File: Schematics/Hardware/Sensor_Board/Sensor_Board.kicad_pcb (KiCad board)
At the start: 2 copper layers, 115.5 x 152.7 mm, 99 parts, among them J1 Conn_02x13_Odd_Even, J2 Conn_02x20_Odd_Even, U1 CAP1188-1-CP-TR, U2 CAP1188-1-CP-TR, U3 CAP1188-1-CP-TR, U4 LCD

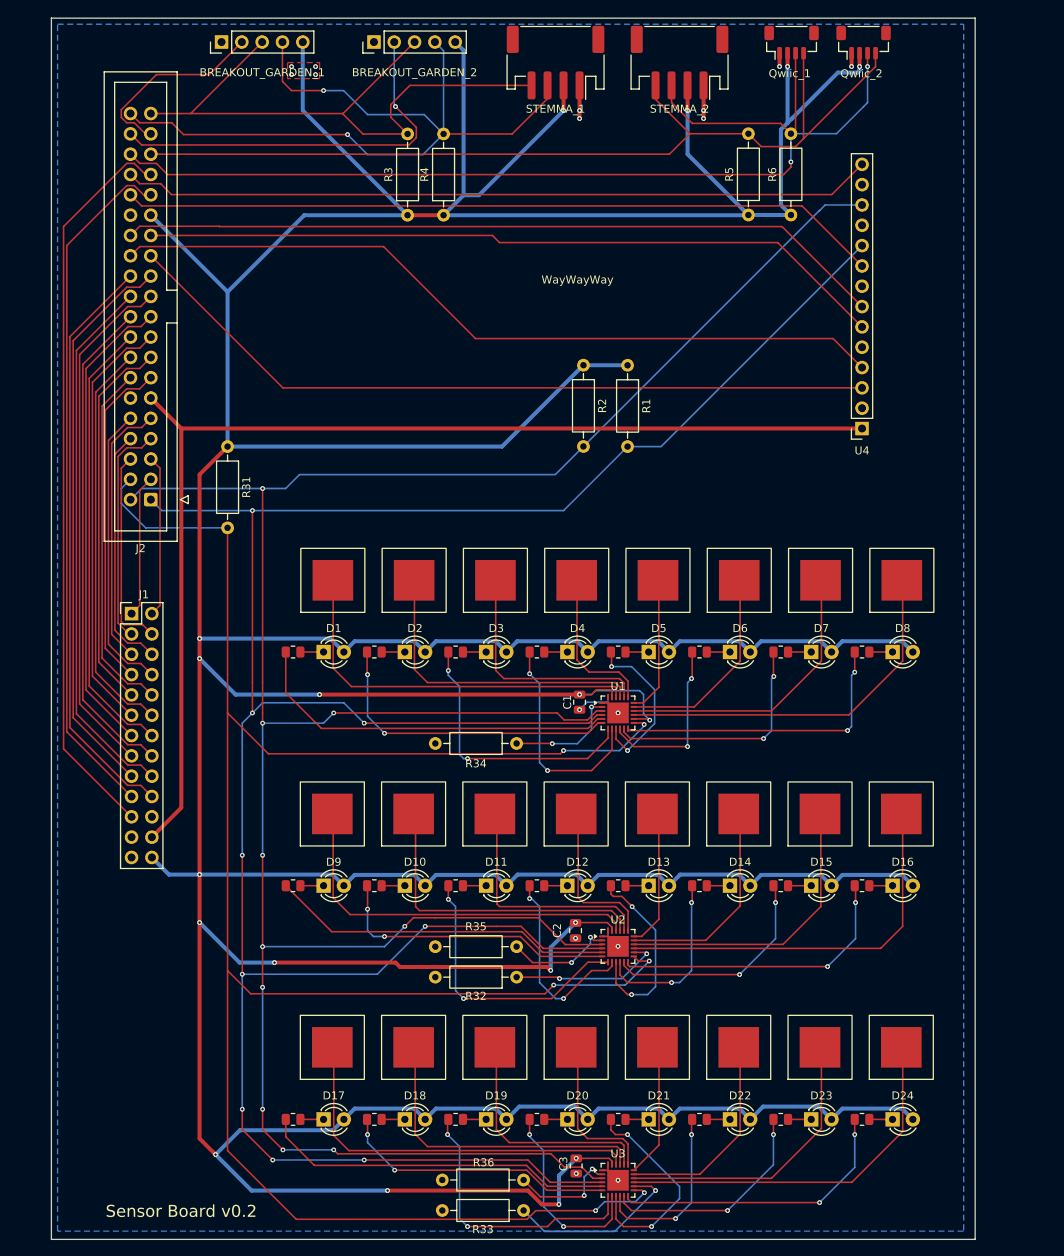
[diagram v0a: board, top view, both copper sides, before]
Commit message: Updated Sensor board schematic/PCB
Still need to double check STEMMA connector and LCD standoff placement.
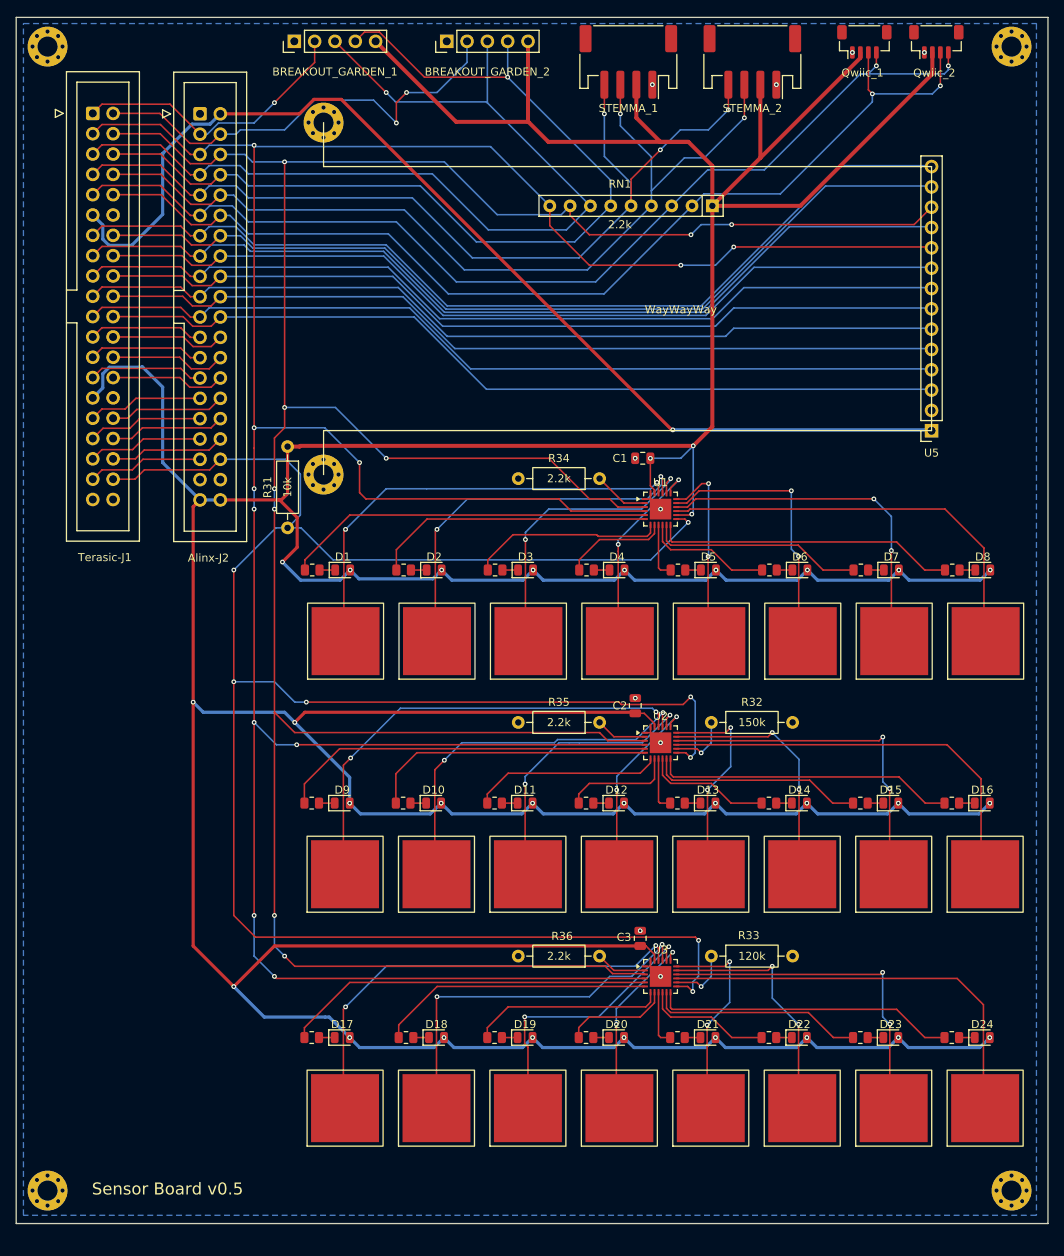
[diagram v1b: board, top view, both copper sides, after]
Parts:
- removed J1: Conn_02x13_Odd_Even, Connector_PinHeader_2.54mm:PinHeader_2x13_P2.54mm_Vertical
- removed R1, R2, R3, R4, R5, R6: 2.2k, Resistor_THT:R_Axial_DIN0207_L6.3mm_D2.5mm_P10.16mm_Horizontal
- removed U4: LCD, Connector_PinSocket_2.54mm:PinSocket_1x14_P2.54mm_Vertical
- added Alinx-J2: Conn_02x20_Odd_Even, Connector_IDC:IDC-Header_2x20_P2.54mm_Vertical, F.Cu at (48.1, 39.4)
- added H1: MountingHole_Pad, MountingHole:MountingHole_2.5mm_Pad_Via, F.Cu at (29.0, 31.0)
- added H2: MountingHole_Pad, MountingHole:MountingHole_2.5mm_Pad_Via, F.Cu at (149.5, 31.0)
- added H3: MountingHole_Pad, MountingHole:MountingHole_2.5mm_Pad_Via, F.Cu at (149.5, 174.0)
- added H4: MountingHole_Pad, MountingHole:MountingHole_2.5mm_Pad_Via, F.Cu at (29.0, 174.0)
- added H5: MountingHole_Pad, MountingHole:MountingHole_2.5mm_Pad_Via, F.Cu at (63.5, 40.5)
- added H6: MountingHole_Pad, MountingHole:MountingHole_2.5mm_Pad_Via, F.Cu at (63.5, 84.5)
- added RN1: 2.2k, Resistor_THT:R_Array_SIP9, F.Cu at (112.1, 50.9)
- added U5: LCD, Connector_PinSocket_2.54mm:PinSocket_1x14_P2.54mm_Vertical, F.Cu at (139.5, 79.0)
- D1, D10, D11, D12, D13, D14, D15, D16, D17, D18, D19, D2, D20, D21, D22, D23, D24, D3, D4, D5, D6, D7, D8, D9: footprint LED_THT:LED_D3.0mm -> Diode_SMD:D_0805_2012Metric
- moved Terasic-J1 48.8 mm to (34.7, 39.4), turned to 0 degrees
- moved R32 40.1 mm to (112.0, 115.5), turned to 0 degrees
- moved R33 39.5 mm to (112.0, 144.7), turned to 0 degrees
- moved R34 34.7 mm to (98.0, 85.0)
- moved C1 31.5 mm to (103.4, 82.5), turned to 180 degrees
- moved R35 29.9 mm to (98.0, 115.5)
- moved R36 29.6 mm to (98.0, 144.7)
- moved C3 29.6 mm to (103.1, 142.5), turned to 90 degrees
- moved C2 29.1 mm to (102.5, 113.4), turned to 90 degrees
- moved U3 26.0 mm to (105.6, 147.2)
- moved U1 26.0 mm to (105.6, 88.8)
- moved U2 26.0 mm to (105.6, 118.0)
- moved R14 15.2 mm to (142.0, 125.6)
- moved D16 15.2 mm to (145.8, 125.6)
- moved D8 15.2 mm to (145.9, 96.4)
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- renumbered J2 to Terasic-J1
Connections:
- BREAKOUT_GARDEN_1 pad 2: GPIO32 (AF20) (AB3) -> GPIO0 (AB22) (V10) (1N)
- BREAKOUT_GARDEN_1 pad 3: GPIO34 (AH23) (AB2) -> GPIO4 (AC21) (V8) (3N)
- BREAKOUT_GARDEN_1 pad 4: GPIO35 (AG26) (AA2) -> GPIO5 (Y16) (W8) (3P)
- BREAKOUT_GARDEN_2 pad 2: GPIO33 (AH26) (Y3) -> GPIO1 (AC15) (W10) (1P)
- BREAKOUT_GARDEN_2 pad 3: GPIO34 (AH23) (AB2) -> GPIO4 (AC21) (V8) (3N)
- BREAKOUT_GARDEN_2 pad 4: GPIO35 (AG26) (AA2) -> GPIO5 (Y16) (W8) (3P)
- Qwiic_1 pad 3: GPIO31 (AG23) (Y4) -> GPIO9 (AE15) (V5) (5P)
- Qwiic_1 pad 4: GPIO30 (AE20) (AA5) -> GPIO8 (AD15) (W6) (5N)
- Qwiic_2 pad 3: GPIO31 (AG23) (Y4) -> GPIO9 (AE15) (V5) (5P)
- Qwiic_2 pad 4: GPIO30 (AE20) (AA5) -> GPIO8 (AD15) (W6) (5N)
- R31 pad 2: GPIO3 (Y17) (W9) -> GPIO33 (AH26) (Y3) (17P)
- STEMMA_1 pad 3: GPIO35 (AG26) (AA2) -> GPIO7 (AE16) (W7) (4P)
- STEMMA_1 pad 4: GPIO34 (AH23) (AB2) -> GPIO6 (AD21) (V7) (4N)
- STEMMA_2 pad 3: GPIO31 (AG23) (Y4) -> GPIO7 (AE16) (W7) (4P)
- STEMMA_2 pad 4: GPIO30 (AE20) (AA5) -> GPIO6 (AD21) (V7) (4N)
- Terasic-J1 pad 1: GPIO0 (AB22) (V10) -> GPIO0 (AB22) (V10) (1N)
- Terasic-J1 pad 10: GPIO9 (AE15) (V5) -> GPIO9 (AE15) (V5) (5P)
- Terasic-J1 pad 13: GPIO10 (AC19) (W5) -> GPIO10 (AC19) (W5) (6N)
- Terasic-J1 pad 14: GPIO11 (AF16) (AA15) -> GPIO11 (AF16) (AA15) (6P)
- Terasic-J1 pad 15: GPIO12 (AD19) (AA14) -> GPIO12 (AD19) (AA14) (7N)
- Terasic-J1 pad 16: GPIO13 (AF15) (W13) -> GPIO13 (AF15) (W13) (7P)
- Terasic-J1 pad 17: GPIO14 (AF24) (W12) -> GPIO14 (AF24) (W12) (8N)
- Terasic-J1 pad 18: GPIO15 (AE21) (AB13) -> GPIO15 (AE21) (AB13) (8P)
- Terasic-J1 pad 19: GPIO16 (AF25) (AB12) -> GPIO16 (AF25) (AB12) (9N)
- Terasic-J1 pad 2: GPIO1 (AC15) (W10) -> GPIO1 (AC15) (W10) (1P)
- Terasic-J1 pad 20: GPIO17 (AC22) (Y11) -> GPIO17 (AC22) (Y11) (9P)
- Terasic-J1 pad 21: GPIO18 (AE22) (AB11) -> GPIO18 (AE22) (AB11) (10N)
- Terasic-J1 pad 22: GPIO19 (AF21) (W11) -> GPIO19 (AF21) (W11) (10P)
- Terasic-J1 pad 23: GPIO20 (AF22) (AB10) -> GPIO20 (AF22) (AB10) (11N)
- Terasic-J1 pad 24: GPIO21 (AD22) (AA10) -> GPIO21 (AD22) (AA10) (11P)
- Terasic-J1 pad 25: GPIO22 (AG25) (AA9) -> GPIO22 (AG25) (AA9) (12N)
- Terasic-J1 pad 26: GPIO23 (AD25) (Y8) -> GPIO23 (AD25) (Y8) (12P)
- Terasic-J1 pad 27: GPIO24 (AH25) (AA8) -> GPIO24 (AH25) (AA8) (13N)
- Terasic-J1 pad 28: GPIO25 (AE25) (Y7) -> GPIO25 (AE25) (Y7) (13P)
- Terasic-J1 pad 3: GPIO2 (AB21) (V9) -> GPIO2 (AB21) (V9) (2N)
- Terasic-J1 pad 31: GPIO26 (AG22) (AA7) -> GPIO26 (AG22) (AA7) (14N)
- Terasic-J1 pad 32: GPIO27 (AE24) (Y6) -> GPIO27 (AE24) (Y6) (14P)
- Terasic-J1 pad 33: GPIO28 (AH22) (AA6) -> GPIO28 (AH22) (AA6) (15N)
- Terasic-J1 pad 34: GPIO29 (AF26) (Y5) -> GPIO29 (AF26) (Y5) (15P)
- Terasic-J1 pad 35: GPIO30 (AE20) (AA5) -> GPIO30 (AE20) (AA5) (16N)
- Terasic-J1 pad 36: GPIO31 (AG23) (Y4) -> GPIO31 (AG23) (Y4) (16P)
- Terasic-J1 pad 37: GPIO32 (AF20) (AB3) -> GPIO32 (AF20) (AB3) (17N)
- Terasic-J1 pad 38: GPIO33 (AH26) (Y3) -> GPIO33 (AH26) (Y3) (17P)
- Terasic-J1 pad 39: GPIO34 (AH23) (AB2) -> GPIO34 (AH23) (AB2) (NC)
- Terasic-J1 pad 4: GPIO3 (Y17) (W9) -> GPIO3 (Y17) (W9) (2P)
- Terasic-J1 pad 40: GPIO35 (AG26) (AA2) -> GPIO35 (AG26) (AA2) (NC)
- Terasic-J1 pad 5: GPIO4 (AC21) (V8) -> GPIO4 (AC21) (V8) (3N)
- Terasic-J1 pad 6: GPIO5 (Y16) (W8) -> GPIO5 (Y16) (W8) (3P)
- Terasic-J1 pad 7: GPIO6 (AD21) (V7) -> GPIO6 (AD21) (V7) (4N)
- Terasic-J1 pad 8: GPIO7 (AE16) (W7) -> GPIO7 (AE16) (W7) (4P)
- Terasic-J1 pad 9: GPIO8 (AD15) (W6) -> GPIO8 (AD15) (W6) (5N)
- U1 pad 13: GPIO3 (Y17) (W9) -> GPIO33 (AH26) (Y3) (17P)
- U1 pad 3: GPIO1 (AC15) (W10) -> GPIO3 (Y17) (W9) (2P)
- U1 pad 4: GPIO0 (AB22) (V10) -> GPIO2 (AB21) (V9) (2N)
- U2 pad 13: GPIO3 (Y17) (W9) -> GPIO33 (AH26) (Y3) (17P)
- U2 pad 3: GPIO1 (AC15) (W10) -> GPIO3 (Y17) (W9) (2P)
- U2 pad 4: GPIO0 (AB22) (V10) -> GPIO2 (AB21) (V9) (2N)
- U3 pad 13: GPIO3 (Y17) (W9) -> GPIO33 (AH26) (Y3) (17P)
- U3 pad 3: GPIO1 (AC15) (W10) -> GPIO3 (Y17) (W9) (2P)
- U3 pad 4: GPIO0 (AB22) (V10) -> GPIO2 (AB21) (V9) (2N)
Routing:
- net GPIO2 (AB21) (V9) (2N): track 0.00 -> 372.7 mm, vias 0 -> 11
- net GPIO3 (Y17) (W9) (2P): track 0.00 -> 355.9 mm, vias 0 -> 9
- net GPIO0 (AB22) (V10): track 323.2 -> 0.00 mm, vias 9 -> 0
- net GPIO1 (AC15) (W10): track 321.0 -> 0.00 mm, vias 10 -> 0
- net GPIO33 (AH26) (Y3) (17P): track 0.00 -> 277.2 mm, vias 0 -> 8
- net GPIO3 (Y17) (W9): track 269.5 -> 0.00 mm, vias 6 -> 0
- net GPIO31 (AG23) (Y4): track 134.5 -> 0.00 mm, vias 2 -> 0
- net GPIO8 (AD15) (W6) (5N): track 0.00 -> 130.6 mm, vias 0 -> 2
- net GPIO9 (AE15) (V5) (5P): track 0.00 -> 130.4 mm, vias 0 -> 2
- net GPIO10 (AC19) (W5) (6N): track 0.00 -> 117.8 mm
- net GPIO4 (AC21) (V8) (3N): track 0.00 -> 117.4 mm, vias 0 -> 1
- net GPIO5 (Y16) (W8) (3P): track 0.00 -> 117.3 mm, vias 0 -> 1
- net GPIO30 (AE20) (AA5): track 116.6 -> 0.00 mm
- net GPIO6 (AD21) (V7) (4N): track 0.00 -> 115.0 mm, vias 0 -> 3
- net GPIO12 (AD19) (AA14) (7N): track 0.00 -> 114.4 mm
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- removed copper zone on F.Cu, net GND
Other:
- board size 115.5 x 152.7 mm -> 129 x 150.8 mm
- board text added: "Sensor Board v0.5"
- board text removed: "Sensor Board v0.2"

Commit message: Added
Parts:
- removed U5: LCD, Connector_PinSocket_2.54mm:PinSocket_1x14_P2.54mm_Vertical
- added H7: MountingHole_Pad, MountingHole:MountingHole_2.5mm_Pad_Via, F.Cu at (134.5, 84.5)
- added H8: MountingHole_Pad, MountingHole:MountingHole_2.5mm_Pad_Via, F.Cu at (134.5, 40.5)
- added J3: Conn_01x14, Connector_PinSocket_2.54mm:PinSocket_1x14_P2.54mm_Vertical, F.Cu at (139.5, 79.0)
- Qwiic_1, Qwiic_2: footprint Connector_JST:JST_SH_BM04B-SRSS-TB_1x04-1MP_P1.00mm_Vertical -> Connector_JST:JST_SH_SM04B-SRSS-TB_1x04-1MP_P1.00mm_Horizontal
- moved Cap_pad1 21.2 mm to (45.1, 105.5)
- moved Cap_pad17 21.2 mm to (45.0, 163.5), turned to 0 degrees
- moved Cap_pad9 21.1 mm to (45.1, 134.5)
- moved R29 20.8 mm to (41.3, 97.0)
- moved D1 20.8 mm to (45.1, 97.0)
- moved R21 20.8 mm to (41.3, 126.0)
- moved D9 20.8 mm to (45.1, 126.0)
- moved R13 20.8 mm to (41.3, 155.0)
- moved D17 20.8 mm to (45.1, 155.0)
- moved Cap_pad2 18.1 mm to (59.6, 105.5)
- moved Cap_pad18 18.1 mm to (59.5, 163.5), turned to 0 degrees
- moved Cap_pad10 18.1 mm to (59.6, 134.5)
- moved D2 17.8 mm to (59.6, 97.0)
- moved R28 17.8 mm to (55.8, 97.0)
- moved D10 17.7 mm to (59.6, 126.0)
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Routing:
- net +3.3V: track 788.2 -> 892.4 mm
- net GPIO3 (Y17) (W9) (2P): track 355.9 -> 416.4 mm
- net GPIO33 (AH26) (Y3) (17P): track 277.2 -> 335.8 mm
- net GPIO2 (AB21) (V9) (2N): track 372.7 -> 424.5 mm
- net /3xCAP1188/LED2.1: track 46.8 -> 68.3 mm
- net /3xCAP1188/LED1.1: track 46.1 -> 66.6 mm
- net /3xCAP1188/LED3.1: track 46.1 -> 66.2 mm
- net /3xCAP1188/CS2.1: track 57.9 -> 77.9 mm
- net /3xCAP1188/CS3.1: track 56.8 -> 76.6 mm
- net /3xCAP1188/CS1.1: track 56.9 -> 75.2 mm
- net /3xCAP1188/LED1.2: track 35.2 -> 52.2 mm
- net /3xCAP1188/LED2.2: track 35.9 -> 52.7 mm
- net /3xCAP1188/LED3.2: track 34.3 -> 51.0 mm
- net /3xCAP1188/CS2.2: track 46.5 -> 62.8 mm
- net /3xCAP1188/CS3.2: track 47.0 -> 62.5 mm
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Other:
- board size 129 x 150.8 mm -> 129 x 150.9 mm

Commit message: Add files via upload
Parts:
- added G***: LOGO, LOGO, F.Cu at (89.5, 173.5)
- added G***: LOGO, LOGO, B.Cu at (134.0, 169.0)
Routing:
- net +3.3V: track 892.4 -> 895.0 mm
- net GPIO4 (AC21) (V8) (3N): track 117.4 -> 118.4 mm
- net /3xCAP1188/CS3.8: track 52.7 -> 51.7 mm
- net /3xCAP1188/LED3.6: track 10.6 -> 11.5 mm
- net +5V: track 136.7 -> 137.6 mm
- net GPIO0 (AB22) (V10) (1N): track 34.7 -> 35.6 mm
- net /3xCAP1188/LED3.4: track 23.7 -> 24.5 mm
- net /3xCAP1188/LED3.3: track 37.7 -> 38.4 mm
- net /3xCAP1188/LED3.2: track 51.0 -> 51.8 mm
- net /3xCAP1188/LED3.1: track 66.2 -> 67.0 mm
- net /3xCAP1188/LED3.8: track 38.5 -> 39.2 mm
- net /3xCAP1188/LED3.7: track 24.6 -> 25.2 mm
- net /3xCAP1188/LED1.7: track 24.7 -> 25.4 mm
- net /3xCAP1188/LED2.8: track 38.6 -> 39.3 mm
- net /3xCAP1188/LED1.8: track 38.7 -> 39.4 mm
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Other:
- board text added: "A.L.D.L."
- board text added: "https://github.com/dmc0022/ALDL_repo"

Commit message: Final Final v0.5 sensor board PCB layout
Fixed incorrect Qwiic and Stemma pinouts.
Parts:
- moved C1 0.67 mm to (102.9, 82.9), turned to 90 degrees
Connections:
- Qwiic_1 pad 1: GND -> GPIO8 (AD15) (W6) (5N)
- Qwiic_1 pad 2: +3.3V -> GPIO9 (AE15) (V5) (5P)
- Qwiic_1 pad 3: GPIO9 (AE15) (V5) (5P) -> +3.3V
- Qwiic_1 pad 4: GPIO8 (AD15) (W6) (5N) -> GND
- Qwiic_2 pad 1: GND -> GPIO8 (AD15) (W6) (5N)
- Qwiic_2 pad 2: +3.3V -> GPIO9 (AE15) (V5) (5P)
- Qwiic_2 pad 3: GPIO9 (AE15) (V5) (5P) -> +3.3V
- Qwiic_2 pad 4: GPIO8 (AD15) (W6) (5N) -> GND
- STEMMA_1 pad 1: GND -> GPIO6 (AD21) (V7) (4N)
- STEMMA_1 pad 2: +3.3V -> GPIO7 (AE16) (W7) (4P)
- STEMMA_1 pad 3: GPIO7 (AE16) (W7) (4P) -> +3.3V
- STEMMA_1 pad 4: GPIO6 (AD21) (V7) (4N) -> GND
- STEMMA_2 pad 1: GND -> GPIO6 (AD21) (V7) (4N)
- STEMMA_2 pad 2: +3.3V -> GPIO7 (AE16) (W7) (4P)
- STEMMA_2 pad 3: GPIO7 (AE16) (W7) (4P) -> +3.3V
- STEMMA_2 pad 4: GPIO6 (AD21) (V7) (4N) -> GND
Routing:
- net GPIO6 (AD21) (V7) (4N): track 115.8 -> 112.0 mm
- net GPIO8 (AD15) (W6) (5N): track 125.7 -> 129.2 mm, vias 2 -> 3
- net GPIO9 (AE15) (V5) (5P): track 128.0 -> 129.0 mm
- net GPIO7 (AE16) (W7) (4P): track 113.6 -> 114.6 mm

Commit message: v0.7 Sensor Board Files
Fixed LCD footprint to now include GND.
Fixed Qwiic connector pinout.
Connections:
- Qwiic_1 pad 1: GPIO8 (AD15) (W6) (5N) -> GND
- Qwiic_1 pad 2: GPIO9 (AE15) (V5) (5P) -> +3.3V
- Qwiic_1 pad 3: +3.3V -> GPIO9 (AE15) (V5) (5P)
- Qwiic_1 pad 4: GND -> GPIO8 (AD15) (W6) (5N)
- Qwiic_2 pad 1: GPIO8 (AD15) (W6) (5N) -> GND
- Qwiic_2 pad 2: GPIO9 (AE15) (V5) (5P) -> +3.3V
- Qwiic_2 pad 3: +3.3V -> GPIO9 (AE15) (V5) (5P)
- Qwiic_2 pad 4: GND -> GPIO8 (AD15) (W6) (5N)
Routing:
- net +3.3V: track 895.5 -> 947.0 mm
- net GND: track 9.65 -> 31.5 mm
- net GPIO8 (AD15) (W6) (5N): track 129.2 -> 125.7 mm, vias 3 -> 2
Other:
- board text added: "Sensor Board v0.7"
- board text removed: "Sensor Board v0.5"
